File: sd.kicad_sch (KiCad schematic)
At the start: 41 parts, among them J2 MicroSD_1140084168, U1 USB2642_ML, Y2 ABM8G-24.000MHZ-18-D2Y-T

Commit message: [#45990] Remove non-sourceable elements from BOMS
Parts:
- TP10, TP11, TP12, TP13, TP7, TP8, TP9: now left out of the parts list
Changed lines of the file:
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@@
   )
   (symbol (lib_id "antmicroTestPoints:TP_0.75mm_SMD") (at 67.945 104.14 180) (unit 1)
-    (in_bom yes) (on_board yes)
+    (in_bom no) (on_board yes)
     (property "Reference" "TP7" (id 0) (at 61.722 104.14 0)
       (effects (font (size 1.27 1.27) (thickness 0.15)))
@@
   )
   (symbol (lib_id "antmicroTestPoints:TP_0.75mm_SMD") (at 67.945 114.3 180) (unit 1)
-    (in_bom yes) (on_board yes)
+    (in_bom no) (on_board yes)
     (property "Reference" "TP10" (id 0) (at 61.722 114.3 0)
       (effects (font (size 1.27 1.27) (thickness 0.15)))
@@
   )
   (symbol (lib_id "antmicroTestPoints:TP_0.75mm_SMD") (at 67.945 121.92 180) (unit 1)
-    (in_bom yes) (on_board yes)
+    (in_bom no) (on_board yes)
     (property "Reference" "TP13" (id 0) (at 61.722 121.92 0)
       (effects (font (size 1.27 1.27) (thickness 0.15)))
@@
   )
   (symbol (lib_id "antmicroTestPoints:TP_0.75mm_SMD") (at 67.945 106.68 180) (unit 1)
-    (in_bom yes) (on_board yes)
+    (in_bom no) (on_board yes)
     (property "Reference" "TP8" (id 0) (at 61.722 106.68 0)
       (effects (font (size 1.27 1.27) (thickness 0.15)))
@@
   )
   (symbol (lib_id "antmicroTestPoints:TP_0.75mm_SMD") (at 67.945 119.38 180) (unit 1)
-    (in_bom yes) (on_board yes)
+    (in_bom no) (on_board yes)
     (property "Reference" "TP12" (id 0) (at 61.722 119.38 0)
       (effects (font (size 1.27 1.27) (thickness 0.15)))
@@
   )
   (symbol (lib_id "antmicroTestPoints:TP_0.75mm_SMD") (at 67.945 109.22 180) (unit 1)
-    (in_bom yes) (on_board yes)
+    (in_bom no) (on_board yes)
     (property "Reference" "TP9" (id 0) (at 61.722 109.22 0)
       (effects (font (size 1.27 1.27) (thickness 0.15)))
@@
   )
   (symbol (lib_id "antmicroTestPoints:TP_0.75mm_SMD") (at 67.945 116.84 180) (unit 1)
-    (in_bom yes) (on_board yes)
+    (in_bom no) (on_board yes)
     (property "Reference" "TP11" (id 0) (at 61.722 116.84 0)
       (effects (font (size 1.27 1.27) (thickness 0.15)))

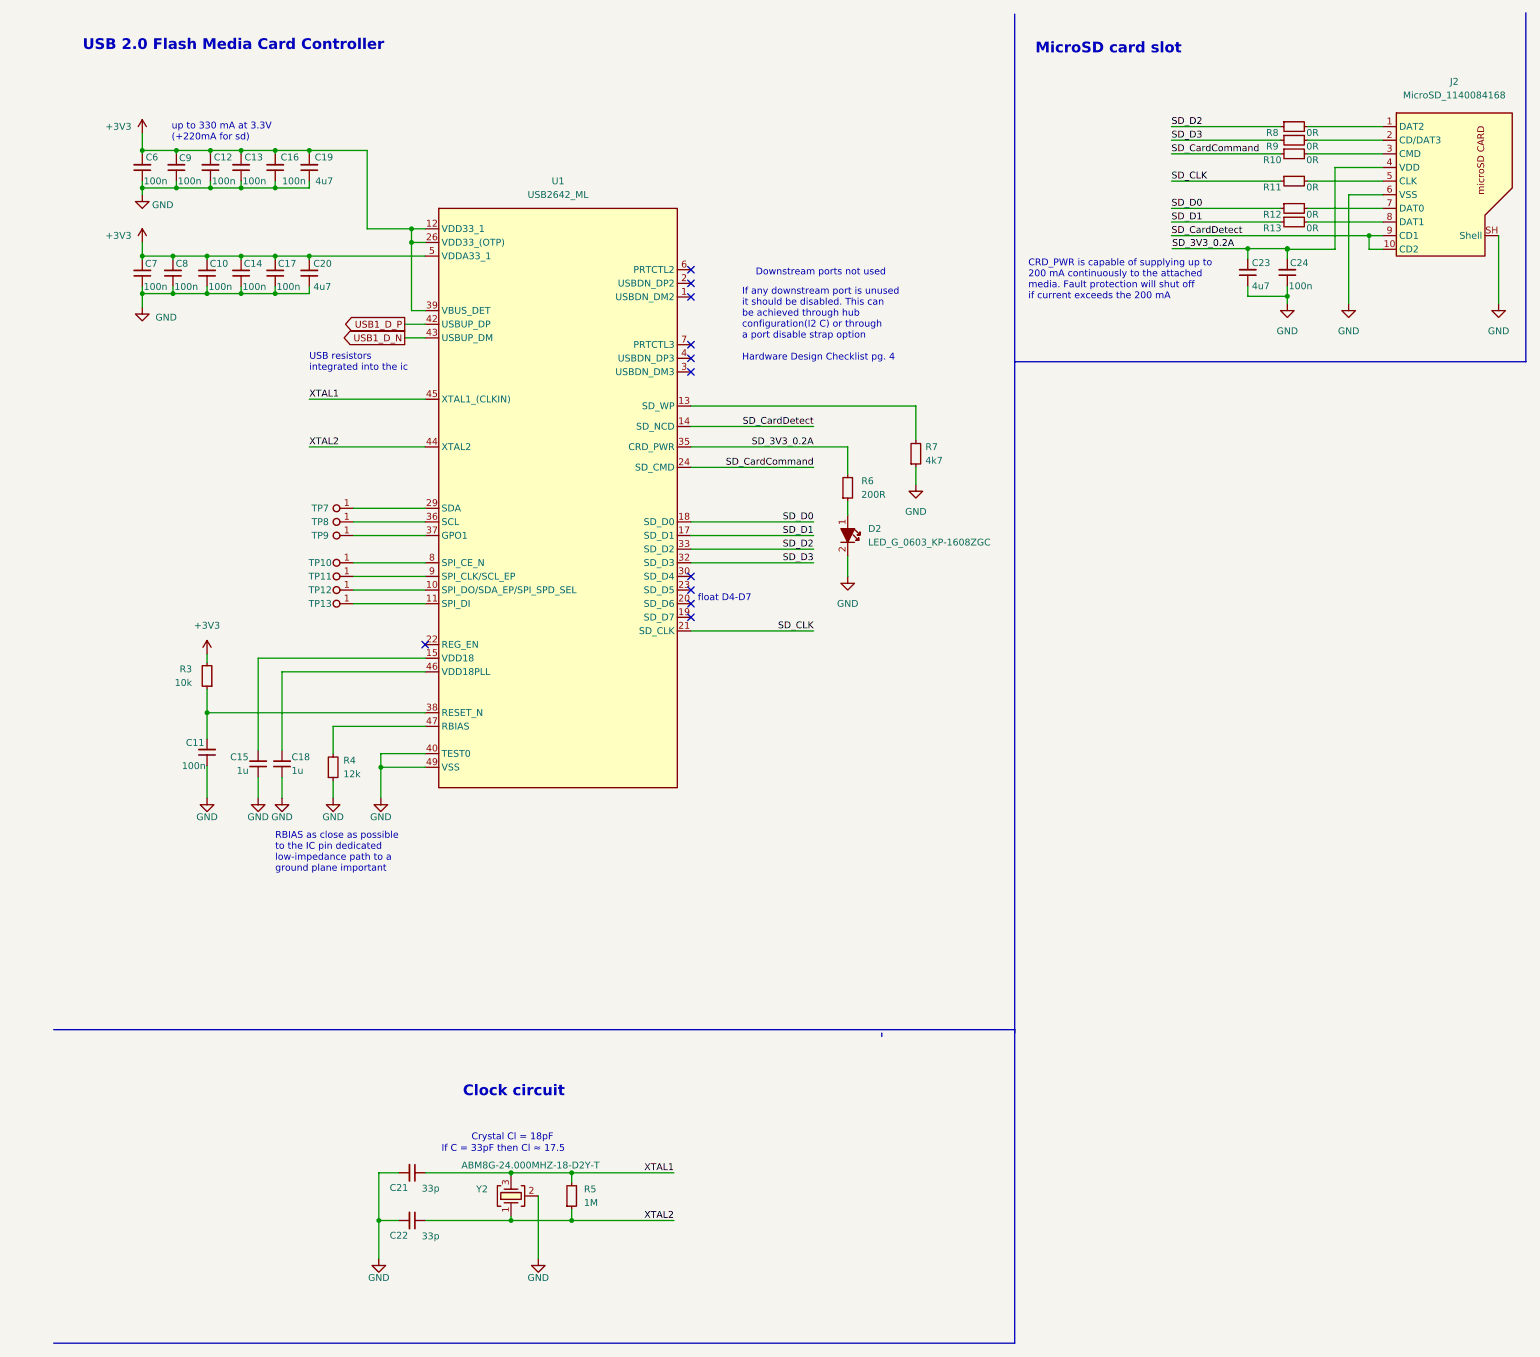
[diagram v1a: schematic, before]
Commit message: [#47315] Fix bug with SD card detect pin
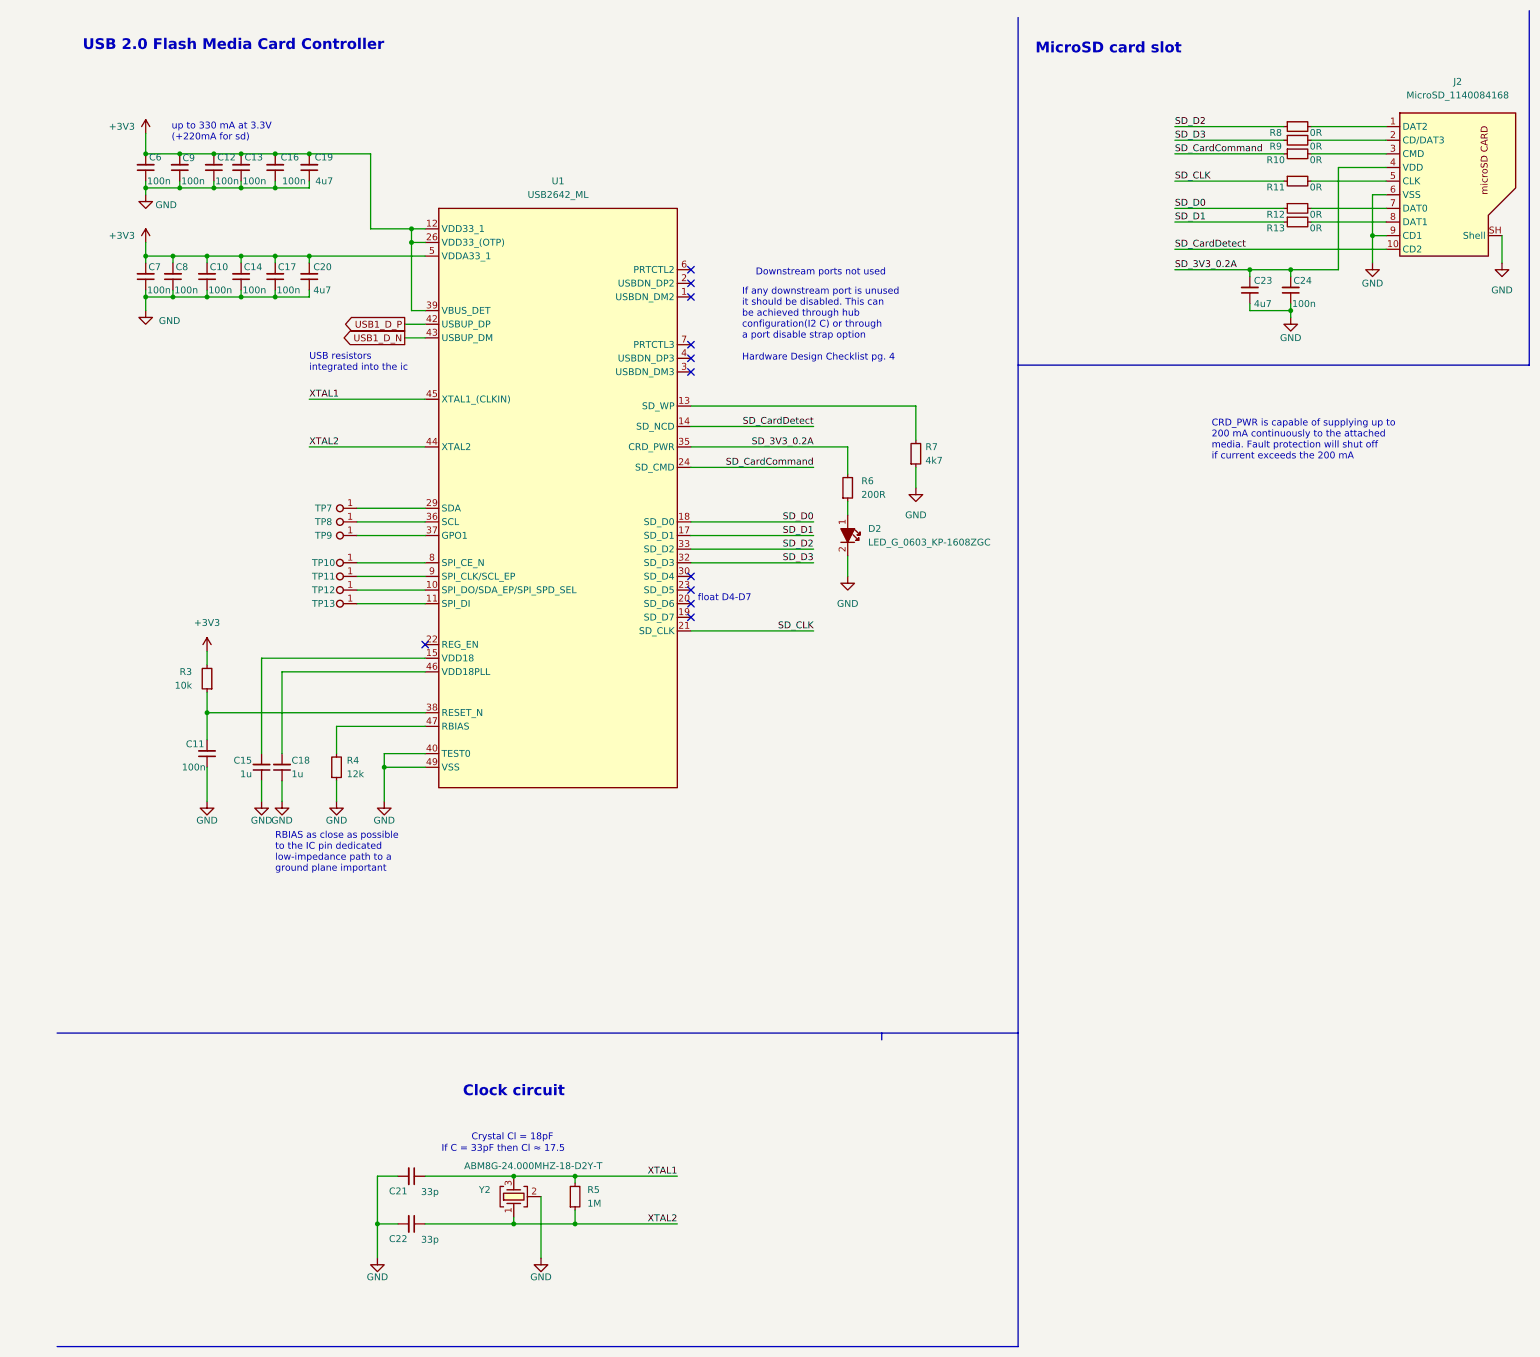
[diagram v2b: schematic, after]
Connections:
- net GND: now also J2.9 (CD1)
- net SD_CardDetect: no longer J2.9 (CD1)
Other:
- moved on the sheet: C10, C12, C14, C15, C17, C18, C20, C21, C22, C23, C24, C6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
